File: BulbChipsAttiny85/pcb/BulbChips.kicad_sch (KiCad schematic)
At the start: 26 parts, among them J1 USB_C_Receptacle_USB2.0_14P, SW1 SW_Push, U1 DMN52D0UV, U2 USBLC6-2P6, U3 S-82A1ACA-I6T1U, U4 ATtiny85-20M, U5 BQ24045DSQR

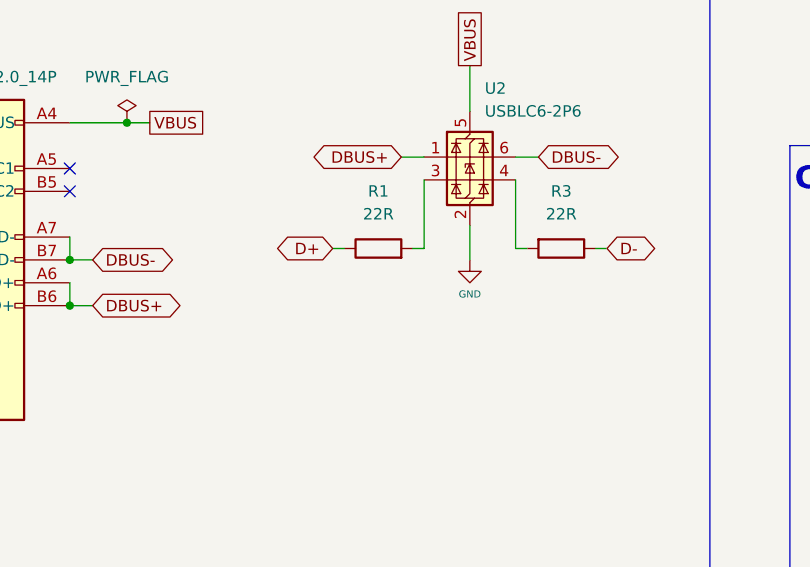
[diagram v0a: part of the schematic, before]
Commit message: updated d+/d- resistor values, and set up low speed usb
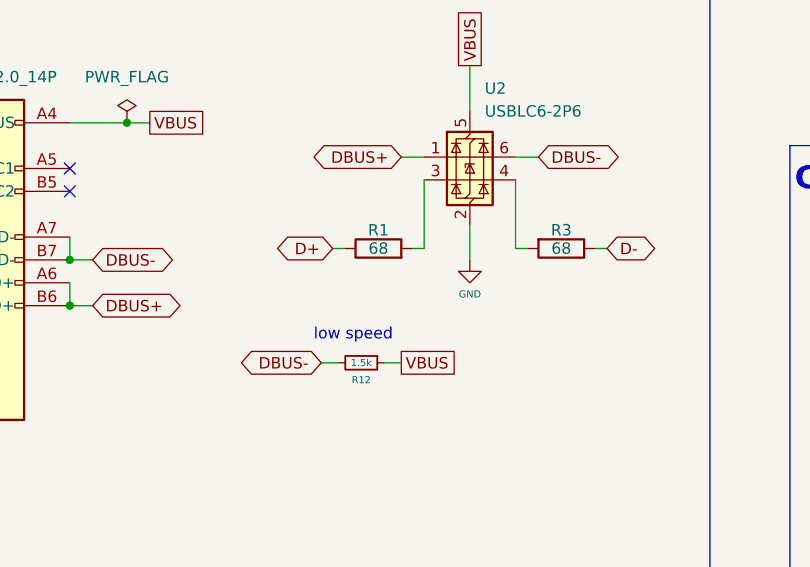
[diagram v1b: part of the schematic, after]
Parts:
- added R12: 1.5k, Resistor_SMD:R_0402_1005Metric, symbol Device:R_Small
- R1, R3: value 22R -> 68
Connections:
- net DBUS-: now also R12.2
- net VBUS: now also R12.1
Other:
- note added: "low speed"
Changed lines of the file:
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@@
 	(wire
 		(pts
+			(xy 93.345 146.05) (xy 91.44 146.05)
+		)
+		(stroke
+			(width 0)
+			(type solid)
+		)
+	)
+	(wire
+		(pts
 			(xy 260.35 146.05) (xy 261.62 146.05)
 		)
@@
 	(wire
 		(pts
+			(xy 100.33 146.05) (xy 98.425 146.05)
+		)
+		(stroke
+			(width 0)
+			(type solid)
+		)
+	)
+	(wire
+		(pts
 			(xy 156.21 274.32) (xy 167.64 274.32)
 		)
@@
 		)
 	)
+	(text "low speed"
+		(exclude_from_sim no)
+		(at 94.996 143.002 0)
+		(effects
+			(font
+				(size 1.27 1.27)
+			)
+		)
+	)
 	(text "BATTERY / PROTECTION IC"
 		(exclude_from_sim no)
@@
 		)
 	)
+	(global_label "DBUS-"
+		(shape bidirectional)
+		(at 91.44 146.05 180)
+		(effects
+			(font
+				(size 1.27 1.27)
+			)
+			(justify right)
+		)
+		(property "Intersheetrefs" "${INTERSHEET_REFS}"
+			(at 80.8505 146.1294 0)
+			(effects
+				(font
+					(size 1.27 1.27)
+				)
+				(justify right)
+				(hide yes)
+			)
+		)
+	)
 	(global_label "D-"
 		(shape bidirectional)
@@
 		)
 	)
+	(global_label "VBUS"
+		(shape passive)
+		(at 100.33 146.05 0)
+		(effects
+			(font
+				(size 1.27 1.27)
+			)
+			(justify left)
+		)
+		(property "Intersheetrefs" "${INTERSHEET_REFS}"
+			(at -243.84 -163.195 0)
+			(effects
+				(font
+					(size 1.27 1.27)
+				)
+				(hide yes)
+			)
+		)
+	)
 	(global_label "Button"
 		(shape passive)
@@
 		(on_board yes)
 		(dnp no)
-		(fields_autoplaced yes)
 		(property "Reference" "R1"
-			(at 97.79 127 90)
+			(at 97.79 131.318 90)
 			(effects
 				(font
@@
 			)
 		)
-		(property "Value" "22R"
-			(at 97.79 129.54 90)
+		(property "Value" "68"
+			(at 97.79 133.35 90)
 			(effects
 				(font
@@
 	)
 	(symbol
+		(lib_id "Device:R_Small")
+		(at 95.885 146.05 270)
+		(unit 1)
+		(exclude_from_sim no)
+		(in_bom yes)
+		(on_board yes)
+		(dnp no)
+		(property "Reference" "R12"
+			(at 95.885 147.955 90)
+			(effects
+				(font
+					(size 0.7874 0.7874)
+				)
+			)
+		)
+		(property "Value" "1.5k"
+			(at 95.885 146.05 90)
+			(effects
+				(font
+					(size 0.7874 0.7874)
+				)
+			)
+		)
+		(property "Footprint" "Resistor_SMD:R_0402_1005Metric"
+			(at 95.885 146.05 0)
+			(effects
+				(font
+					(size 1.27 1.27)
+				)
+				(hide yes)
+			)
+		)
+		(property "Datasheet" "~"
+			(at 95.885 146.05 0)
+			(effects
+				(font
+					(size 1.27 1.27)
+				)
+				(hide yes)
+			)
+		)
+		(property "Description" ""
+			(at 95.885 146.05 0)
+			(effects
+				(font
+					(size 1.27 1.27)
+				)
+				(hide yes)
+			)
+		)
+		(property "Package" "R0402"
+			(at 95.885 146.05 0)
+			(effects
+				(font
+					(size 1.27 1.27)
+				)
+				(hide yes)
+			)
+		)
+		(pin "1"
+		)
+		(pin "2"
+		)
+		(instances
+			(project "BulbChips"
+				(path "/fc2915fa-7a9c-445c-a5d7-b7fdeb691e1a"
+					(reference "R12")
+					(unit 1)
+				)
+			)
+		)
+	)
+	(symbol
 		(lib_id "Power_Protection:USBLC6-2P6")
 		(at 107.95 123.19 0)
@@
 		(on_board yes)
 		(dnp no)
-		(fields_autoplaced yes)
 		(property "Reference" "R3"
-			(at 118.11 127 90)
+			(at 118.11 131.318 90)
 			(effects
 				(font
@@
 			)
 		)
-		(property "Value" "22R"
-			(at 118.11 129.54 90)
+		(property "Value" "68"
+			(at 118.11 133.35 90)
 			(effects
 				(font

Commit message: cleanup
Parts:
- renumbered R12 to R1, R9 to R10, R10 to R11, R11 to R12, R1 to R2, R2 to R3, R3 to R4, R4 to R5, R5 to R6, R6 to R7, R7 to R8, R8 to R9
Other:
- moved on the sheet: R1
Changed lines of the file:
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@@
 	(wire
 		(pts
-			(xy 93.345 146.05) (xy 91.44 146.05)
-		)
-		(stroke
-			(width 0)
-			(type solid)
-		)
-	)
-	(wire
-		(pts
 			(xy 260.35 146.05) (xy 261.62 146.05)
 		)
@@
 	(wire
 		(pts
-			(xy 100.33 146.05) (xy 98.425 146.05)
-		)
-		(stroke
-			(width 0)
-			(type solid)
-		)
-	)
-	(wire
-		(pts
 			(xy 156.21 274.32) (xy 167.64 274.32)
 		)
@@
 	(wire
 		(pts
+			(xy 91.44 146.05) (xy 93.98 146.05)
+		)
+		(stroke
+			(width 0)
+			(type default)
+		)
+	)
+	(wire
+		(pts
 			(xy 219.71 71.12) (xy 222.25 71.12)
 		)
@@
 	(wire
 		(pts
+			(xy 99.06 146.05) (xy 101.6 146.05)
+		)
+		(stroke
+			(width 0)
+			(type default)
+		)
+	)
+	(wire
+		(pts
 			(xy 73.66 264.16) (xy 71.12 264.16)
 		)
@@
 	(global_label "VBUS"
 		(shape passive)
-		(at 100.33 146.05 0)
+		(at 101.6 146.05 0)
 		(effects
 			(font
@@
 		)
 		(property "Intersheetrefs" "${INTERSHEET_REFS}"
-			(at -243.84 -163.195 0)
+			(at -242.57 -163.195 0)
 			(effects
 				(font
@@
 		(dnp no)
 		(fields_autoplaced yes)
-		(property "Reference" "R6"
+		(property "Reference" "R7"
 			(at 180.34 149.86 90)
 			(effects
@@
 			(project ""
 				(path "/fc2915fa-7a9c-445c-a5d7-b7fdeb691e1a"
-					(reference "R6")
+					(reference "R7")
 					(unit 1)
 				)
@@
 		(dnp no)
 		(fields_autoplaced yes)
-		(property "Reference" "R7"
+		(property "Reference" "R8"
 			(at 180.34 158.75 90)
 			(effects
@@
 			(project "BulbChips"
 				(path "/fc2915fa-7a9c-445c-a5d7-b7fdeb691e1a"
-					(reference "R7")
+					(reference "R8")
 					(unit 1)
 				)
@@
 		(dnp no)
 		(fields_autoplaced yes)
-		(property "Reference" "R2"
+		(property "Reference" "R3"
 			(at 104.14 255.27 90)
 			(effects
@@
 			(project ""
 				(path "/fc2915fa-7a9c-445c-a5d7-b7fdeb691e1a"
-					(reference "R2")
+					(reference "R3")
 					(unit 1)
 				)
@@
 		(dnp no)
 		(fields_autoplaced yes)
-		(property "Reference" "R10"
+		(property "Reference" "R11"
 			(at 288.29 87.63 90)
 			(effects
@@
 			(project ""
 				(path "/fc2915fa-7a9c-445c-a5d7-b7fdeb691e1a"
-					(reference "R10")
+					(reference "R11")
 					(unit 1)
 				)
@@
 		(dnp no)
 		(fields_autoplaced yes)
-		(property "Reference" "R9"
+		(property "Reference" "R10"
 			(at 256.54 151.13 90)
 			(effects
@@
 			(project "BulbChips"
 				(path "/fc2915fa-7a9c-445c-a5d7-b7fdeb691e1a"
-					(reference "R9")
+					(reference "R10")
 					(unit 1)
 				)
@@
 		(dnp no)
 		(fields_autoplaced yes)
-		(property "Reference" "R5"
+		(property "Reference" "R6"
 			(at 151.13 267.97 90)
 			(effects
@@
 			(project ""
 				(path "/fc2915fa-7a9c-445c-a5d7-b7fdeb691e1a"
-					(reference "R5")
+					(reference "R6")
 					(unit 1)
 				)
@@
 		(dnp no)
 		(fields_autoplaced yes)
-		(property "Reference" "R11"
+		(property "Reference" "R12"
 			(at 293.37 73.66 90)
 			(effects
@@
 			(project "BulbChips"
 				(path "/fc2915fa-7a9c-445c-a5d7-b7fdeb691e1a"
-					(reference "R11")
+					(reference "R12")
 					(unit 1)
 				)
@@
 		(on_board yes)
 		(dnp no)
-		(property "Reference" "R1"
+		(property "Reference" "R2"
 			(at 97.79 131.318 90)
 			(effects
@@
 			(project "BulbChips"
 				(path "/fc2915fa-7a9c-445c-a5d7-b7fdeb691e1a"
-					(reference "R1")
+					(reference "R2")
 					(unit 1)
 				)
@@
 		(dnp no)
 		(fields_autoplaced yes)
-		(property "Reference" "R8"
+		(property "Reference" "R9"
 			(at 256.54 139.7 90)
 			(effects
@@
 			(project ""
 				(path "/fc2915fa-7a9c-445c-a5d7-b7fdeb691e1a"
-					(reference "R8")
+					(reference "R9")
 					(unit 1)
 				)
@@
 	(symbol
 		(lib_id "Device:R_Small")
-		(at 95.885 146.05 270)
+		(at 96.52 146.05 270)
 		(unit 1)
 		(exclude_from_sim no)
@@
 		(on_board yes)
 		(dnp no)
-		(property "Reference" "R12"
-			(at 95.885 147.955 90)
+		(property "Reference" "R1"
+			(at 96.52 147.955 90)
 			(effects
 				(font
@@
 		)
 		(property "Value" "1.5k"
-			(at 95.885 146.05 90)
+			(at 96.52 146.05 90)
 			(effects
 				(font
@@
 		)
 		(property "Footprint" "Resistor_SMD:R_0402_1005Metric"
-			(at 95.885 146.05 0)
+			(at 96.52 146.05 0)
 			(effects
 				(font
@@
 		)
 		(property "Datasheet" "~"
-			(at 95.885 146.05 0)
+			(at 96.52 146.05 0)
 			(effects
 				(font
@@
 		)
 		(property "Description" ""
-			(at 95.885 146.05 0)
+			(at 96.52 146.05 0)
 			(effects
 				(font
@@
 		)
 		(property "Package" "R0402"
-			(at 95.885 146.05 0)
+			(at 96.52 146.05 0)
 			(effects
 				(font
@@
 			(project "BulbChips"
 				(path "/fc2915fa-7a9c-445c-a5d7-b7fdeb691e1a"
-					(reference "R12")
+					(reference "R1")
 					(unit 1)
 				)
@@
 		(on_board yes)
 		(dnp no)
-		(property "Reference" "R3"
+		(property "Reference" "R4"
 			(at 118.11 131.318 90)
 			(effects
@@
 			(project "BulbChips"
 				(path "/fc2915fa-7a9c-445c-a5d7-b7fdeb691e1a"
-					(reference "R3")
+					(reference "R4")
 					(unit 1)
 				)
@@
 		(dnp no)
 		(fields_autoplaced yes)
-		(property "Reference" "R4"
+		(property "Reference" "R5"
 			(at 133.35 260.35 90)
 			(effects
@@
 			(project ""
 				(path "/fc2915fa-7a9c-445c-a5d7-b7fdeb691e1a"
-					(reference "R4")
+					(reference "R5")
 					(unit 1)
 				)

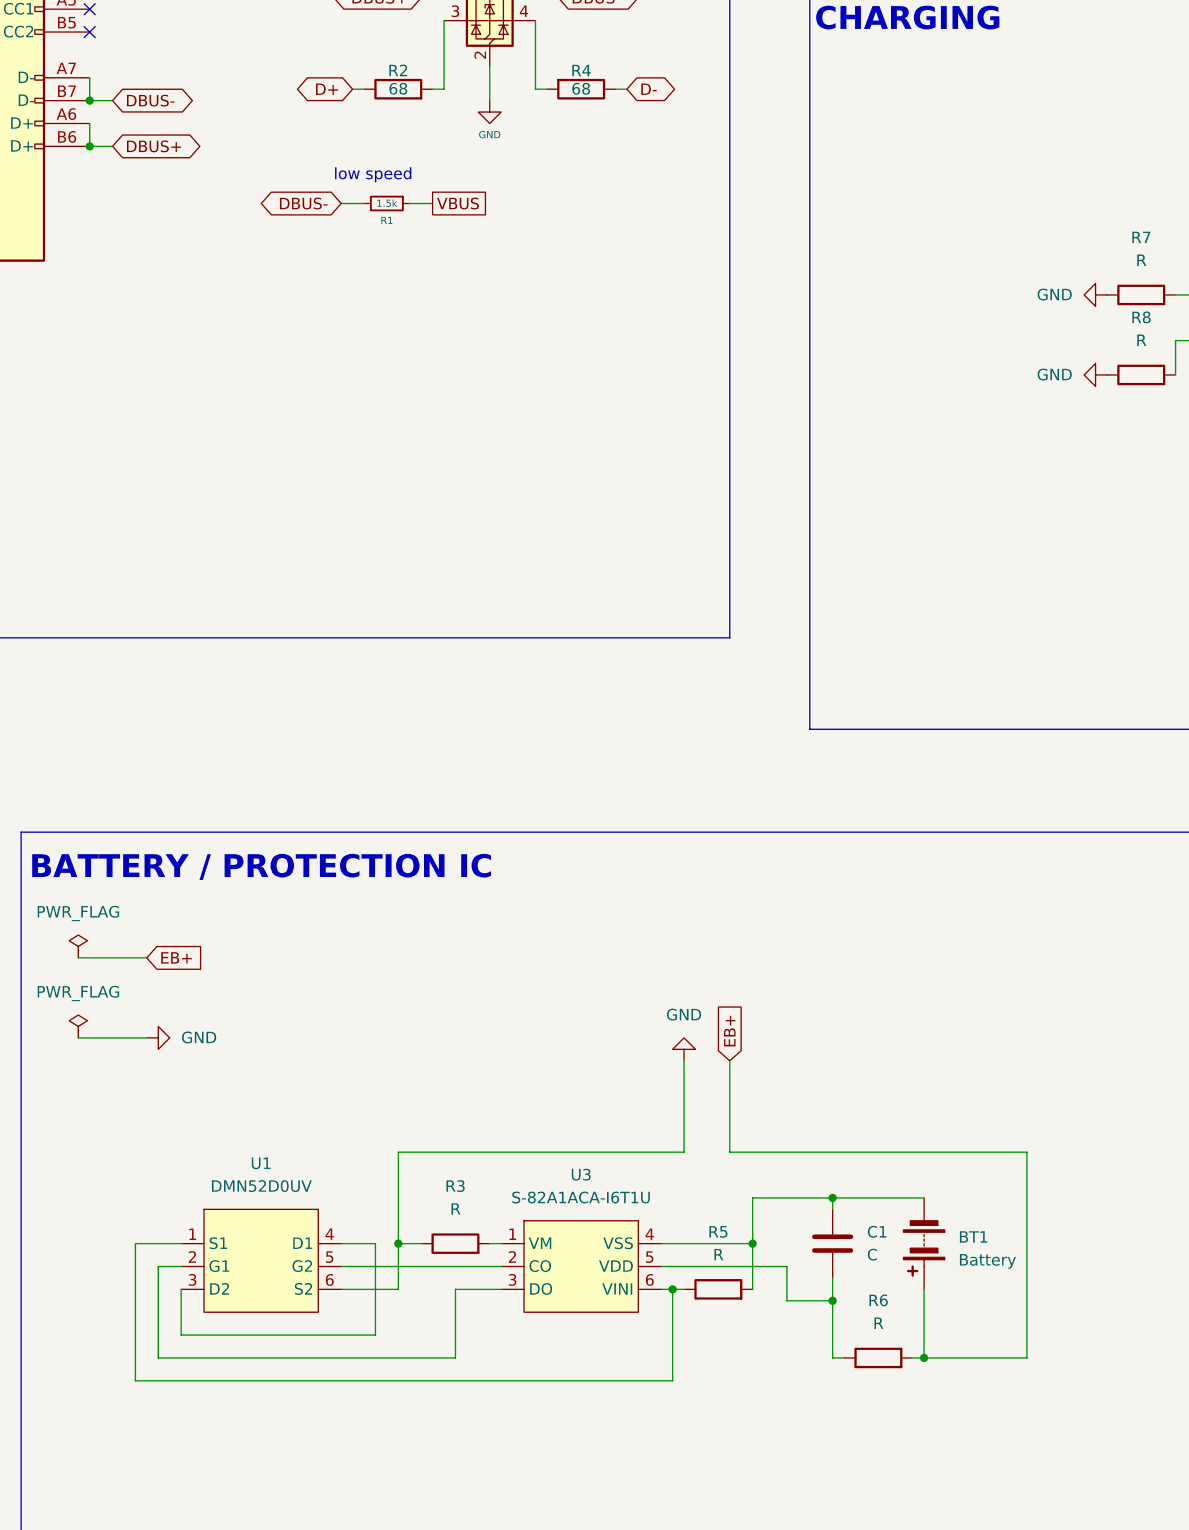
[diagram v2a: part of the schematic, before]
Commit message: added capacitor and resistor values for battery protection circuit
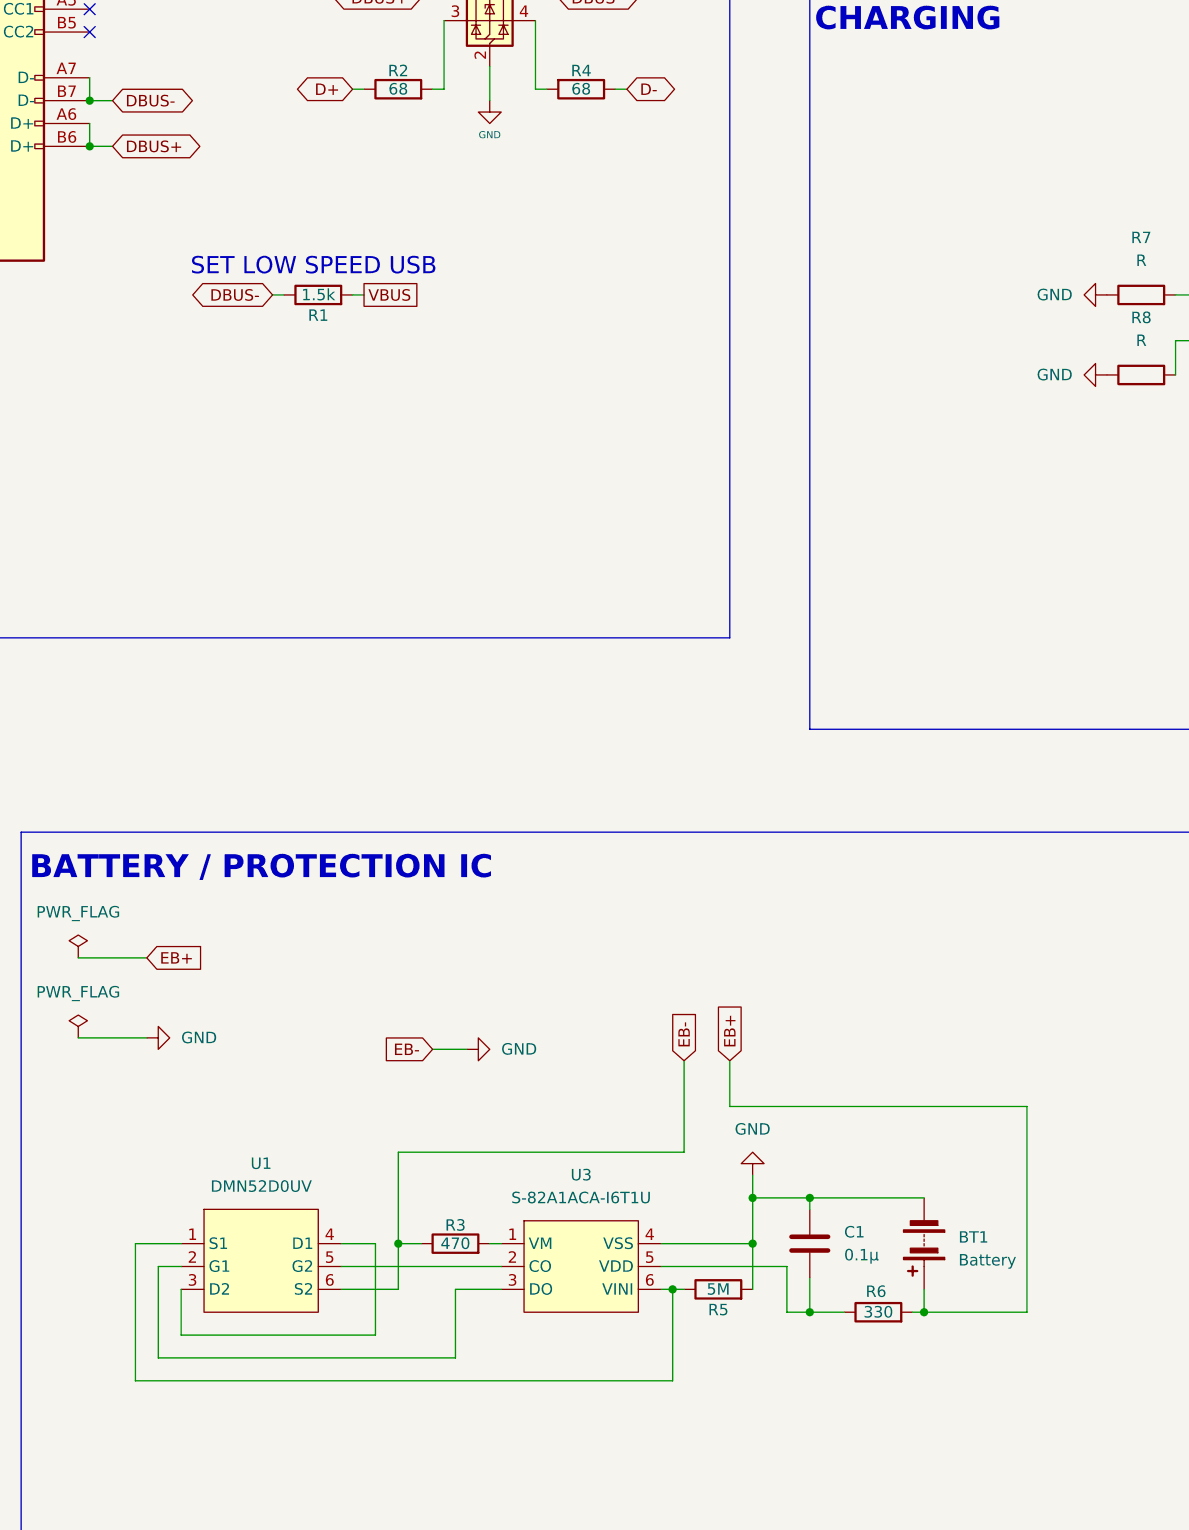
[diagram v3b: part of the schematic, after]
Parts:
- removed R1: 1.5k, Resistor_SMD:R_0402_1005Metric, symbol Device:R_Small
- added R1: 1.5k, symbol Device:R
- C1: value C -> 0.1μ
- R3: value R -> 470
- R5: value R -> 5M
- R6: value R -> 330
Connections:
- net DBUS-: now also R1.1
- net GND: now also BT1.2 (-), C1.1, R5.2, U3.4 (VSS)
- net VBUS: now also R1.2
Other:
- note added: "SET LOW SPEED USB"
- note removed: "low speed"
- moved on the sheet: C1, R6
